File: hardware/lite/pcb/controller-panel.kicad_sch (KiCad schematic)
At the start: 23 parts, among them SW1171 PTS645SL50SMTR92LFS, U1171 SN74AHCT1G125DBVR, U1172 TCA6408ARGTR

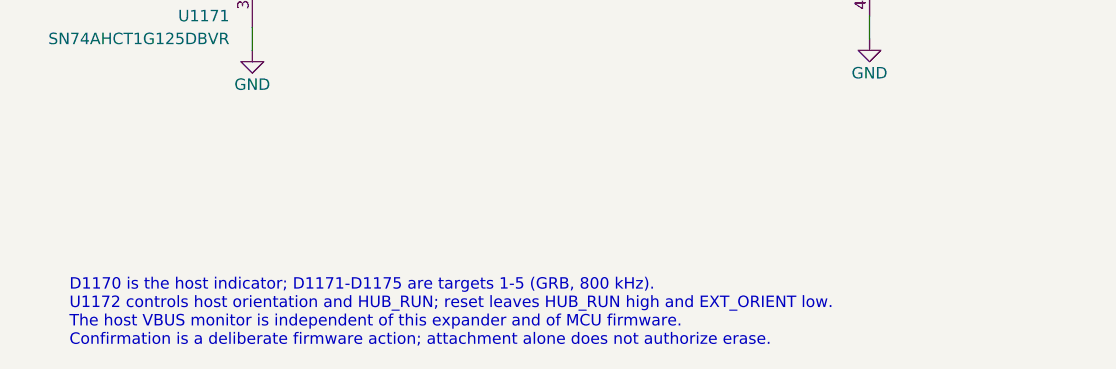
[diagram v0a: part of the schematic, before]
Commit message: feat(hardware): identify system status indicator
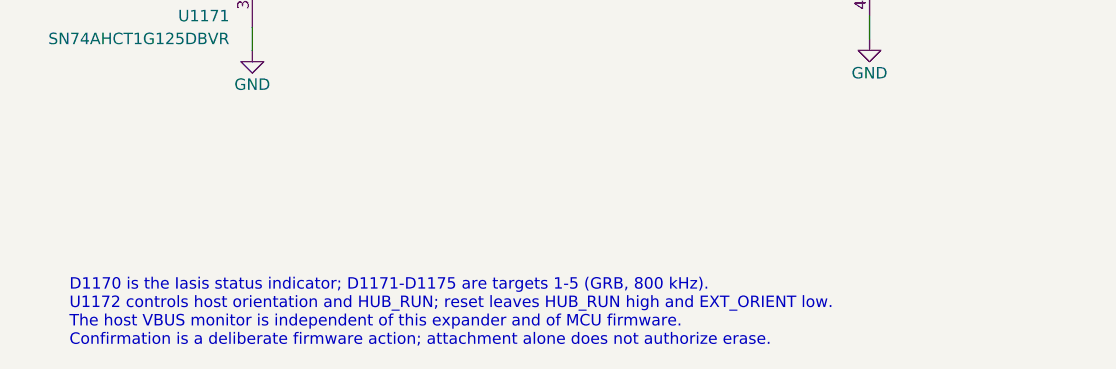
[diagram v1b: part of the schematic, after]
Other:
- note added: "D1170 is the Iasis status indicator; D1171-D1175 are targets 1-5 (GRB, 800 kHz). U1172 controls host orientation and HUB_RUN; reset leaves HUB_RUN high and EXT_ORIENT low. The host VBUS monitor is independent of this expander and of MCU firmware. Confirmation is a deliberate firmware action; attachment alone does not authorize erase."
- note removed: "D1170 is the host indicator; D1171-D1175 are targets 1-5 (GRB, 800 kHz). U1172 controls host orientation and HUB_RUN; reset leaves HUB_RUN high and EXT_ORIENT low. The host VBUS monitor is independent of this expander and of MCU firmware. Confirmation is a deliberate firmware action; attachment alone does not authorize erase."
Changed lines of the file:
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@@
 		(rev "A")
-	)
-	(text "D1170 is the host indicator; D1171-D1175 are targets 1-5 (GRB, 800 kHz).\nU1172 controls host orientation and HUB_RUN; reset leaves HUB_RUN high and EXT_ORIENT low.\nThe host VBUS monitor is independent of this expander and of MCU firmware.\nConfirmation is a deliberate firmware action; attachment alone does not authorize erase."
-		(exclude_from_sim no)
-		(at 25.4 203.2 0)
-		(effects
-			(font
-				(size 1.27 1.27)
-			)
-			(justify left top)
-		)
 	)
 	(text "Port indicators and physical confirmation"
@@
 		)
 	)
+  (text "D1170 is the Iasis status indicator; D1171-D1175 are targets 1-5 (GRB, 800 kHz).\nU1172 controls host orientation and HUB_RUN; reset leaves HUB_RUN high and EXT_ORIENT low.\nThe host VBUS monitor is independent of this expander and of MCU firmware.\nConfirmation is a deliberate firmware action; attachment alone does not authorize erase."
+    (at 25.4 203.2 0)
+    (effects (font (size 1.27 1.27)) (justify left top))
+  )
 	(symbol
 		(lib_id "Device:C")

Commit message: feat(hardware): share brick power across ports and add CM5 link
A connected PD supply now runs the logic through its own buck and feeds
one TPS55288 buck-boost stage per port, so the contract is shared as
5-20 V at up to 5 A per port. The hub's VBUS detect becomes an OR gate,
a host-select mux lets a CM5 side board drive the hub over a 24-pin ZIF
link, and a CM5 variant joins Hub and HubPD.

The board is synced to the schematic and its old routing removed; the
new parts wait below the outline for placement.
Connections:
- net SIDE_PRESENT_N: now reaches U1172.10 (P7)
- no-connect marks 3 -> 2
